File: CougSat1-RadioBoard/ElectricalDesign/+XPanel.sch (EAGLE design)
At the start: 51 parts, among them J1 ADCS Connector, J2 Low Gain +, J3 Low Gain -, J4 Low Gain Coax, J5 GPS Coax, J6 ADCS Connector, U2 MCP1501-18, U3 AD7291

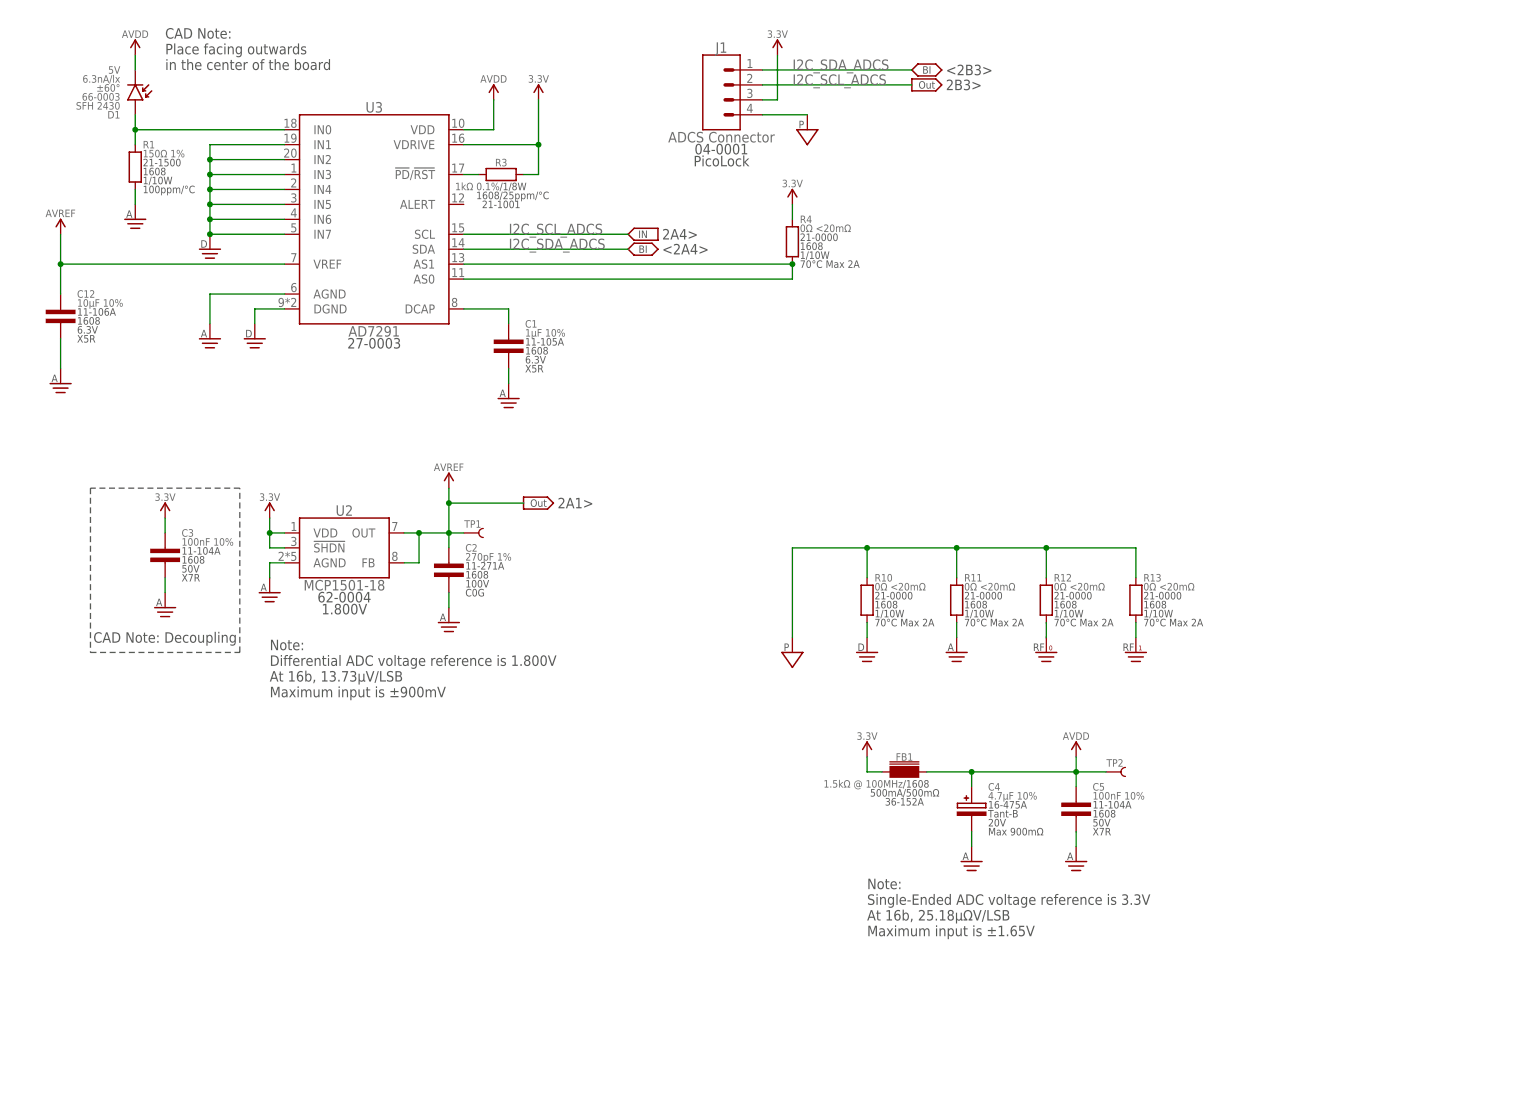
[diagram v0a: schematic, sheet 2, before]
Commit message: Added Thermistors
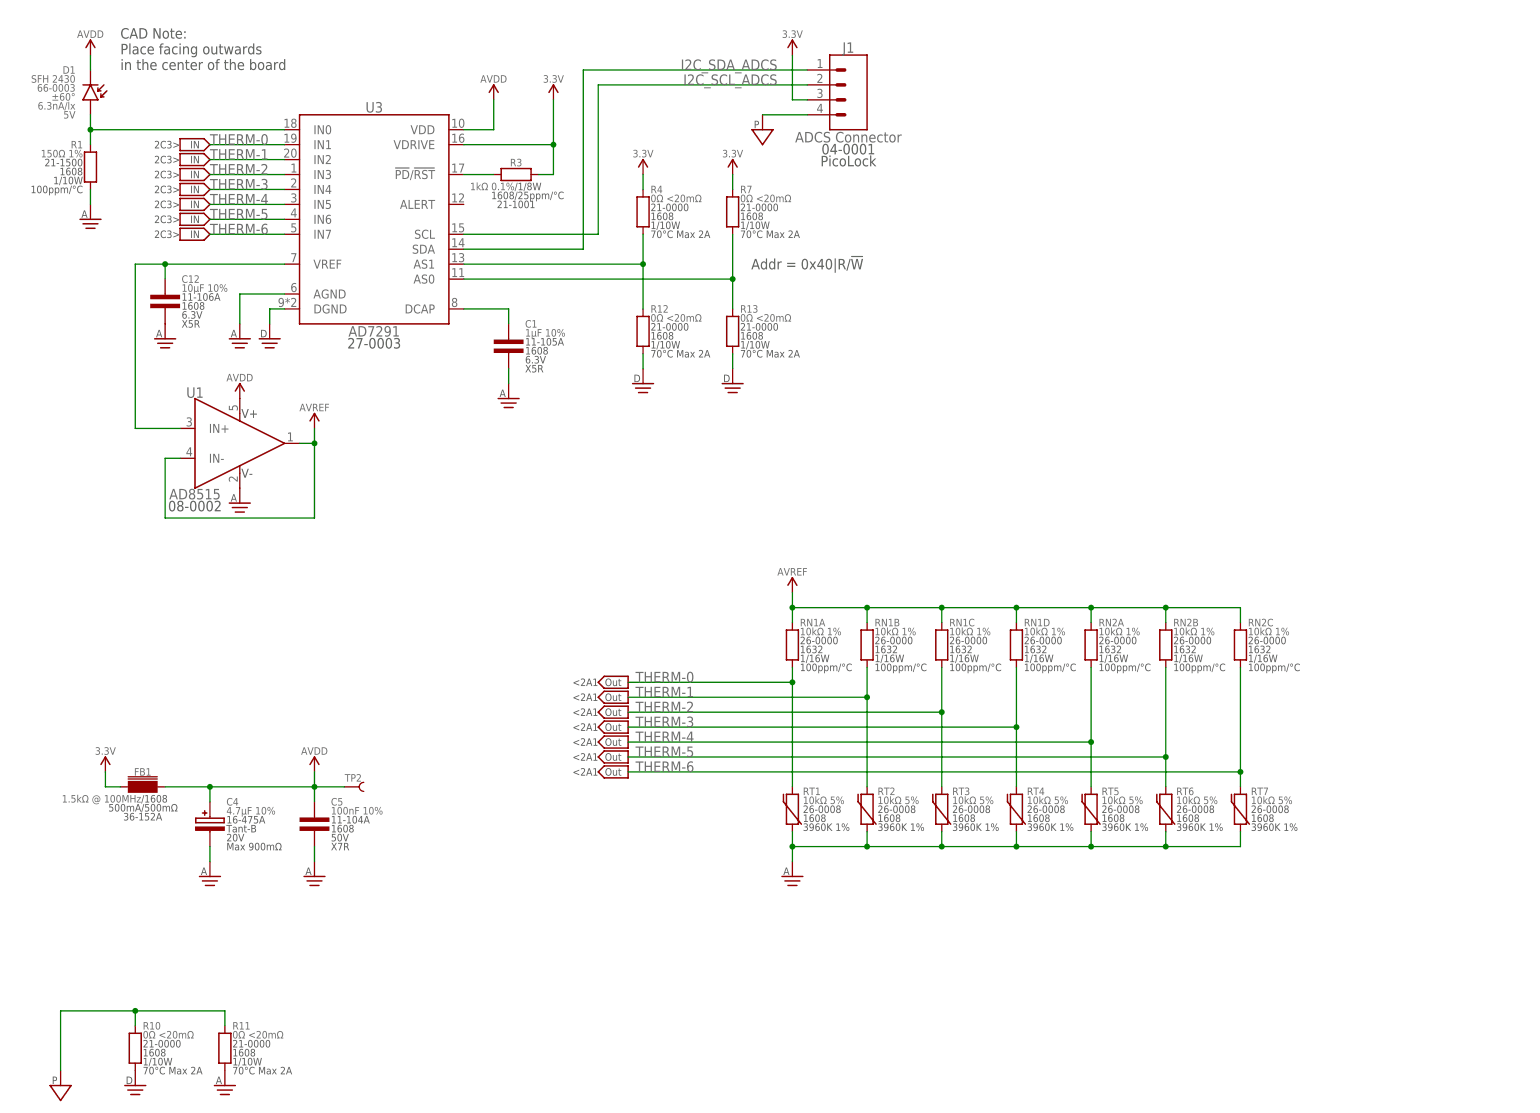
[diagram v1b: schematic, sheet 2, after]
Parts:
- removed C2: 270pF 1%, CougsInSpace-Capacitors:CAP-V-270PF-1608
- removed C3: 100nF 10%, CougsInSpace-Capacitors:CAP-V-100NF-1608
- removed TP1: TEST_POINT-THT-0.7, CougsInSpace-Connectors:TEST_POINT-THT-0.7
- removed U2: MCP1501-18, CougsInSpace-IC-Other:MCP1501-18E/RW
- added R7: 0Ω <20mΩ, CougsInSpace-Resistors:RES-V-0-1608
- added RN1, RN2: 10kΩ 1%, CougsInSpace-Resistors:RES-4-V-10K-1632
- added RT1, RT2, RT3, RT4, RT5, RT6, RT7: 10kΩ 5%, CougsInSpace-Resistors:THERMISTOR-V-10K-1608
- added U1: AD8515, CougsInSpace-IC-Amplifiers:OPAMP-1-AD8515
- J6: value ADCS Connector -> EPS Connector
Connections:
- removed net N$4: R4.1, U3.AS0, U3.AS1
- new net ADC_AS0: R13.2, R7.1, U3.AS0
- new net ADC_AS1: R12.2, R4.1, U3.AS1
- new net AVREF_UNBUF: C12.1, U1.IN+, U3.VREF
- new net THERM-0: RN1A.1, RT1.2, U3.IN1
- new net THERM-1: RN1B.1, RT2.2, U3.IN2
- new net THERM-2: RN1C.1, RT3.2, U3.IN3
- new net THERM-3: RN1D.1, RT4.2, U3.IN4
- new net THERM-4: RN2A.1, RT5.2, U3.IN5
- new net THERM-5: RN2B.1, RT6.2, U3.IN6
- new net THERM-6: RN2C.1, RT7.2, U3.IN7
- net 3.3V: now also R7.2; no longer C3.1, U2.!SHDN, U2.VDD
- net AGND: now also RT1.1, RT2.1, RT3.1, RT4.1, RT5.1, RT6.1, RT7.1, U1.V-; no longer C2.2, C3.2, U2.AGND
- net AVDD: now also U1.V+
- net AVREF: now also RN1A.2, RN1B.2, RN1C.2, RN1D.2, RN2A.2, RN2B.2, RN2C.2, U1.IN-, U1.OUT; no longer C12.1, C2.1, TP1.1, U2.FB, U2.OUT, U3.VREF
- net DGND: now also R12.1, R13.1; no longer U3.IN1, U3.IN2, U3.IN3, U3.IN4, U3.IN5, U3.IN6, U3.IN7
- net PGND: no longer R12.2, R13.2
- net RFGND-0: no longer R12.1
- net RFGND-1: no longer R13.1
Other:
- note added: "2C3>"
- note added: "<2A1"
- note added: "Addr = 0x40|R/!W"
- note added: "I²C"
- note added: "Note: The low gain antenna wraps around posts in these holes which shorts them together. When deployed, the deploy sense pin will be pulled high by the EPS"
- note added: "Page 1: Block Diagram Page 2: Photodiode & ADC Page 3: Antennae Page 4: Mechanical"
- note added: "Photodiode"
- note added: "Thermistors"
- note removed: "2A1>"
- note removed: "2A4>"
- note removed: "2B3>"
- note removed: "3A4>"
- note removed: "<2A4>"
- note removed: "<2B3>"
- note removed: "<3A5"
- note removed: "CAD Note: Decoupling"
- note removed: "Connector: To Avionics"
- note removed: "Note: Differential ADC voltage reference is 1.800V At 16b, 13.73µV/LSB Maximum input is ±900mV"
- note removed: "Note: Single-Ended ADC voltage reference is 3.3V At 16b, 25.18µΩV/LSB Maximum input is ±1.65V"
- note removed: "PC"
- note removed: "Page 1: Block Diagram Page 2: Photodiode Page 3: Antennae Page 4: Mechanical"
- note removed: "Photodiodes"
- moved on the sheet: AE1, C12, C4, C5, D1, FB1, H1, H2, H3, H4, J1, J2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

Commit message: Fixed formatting
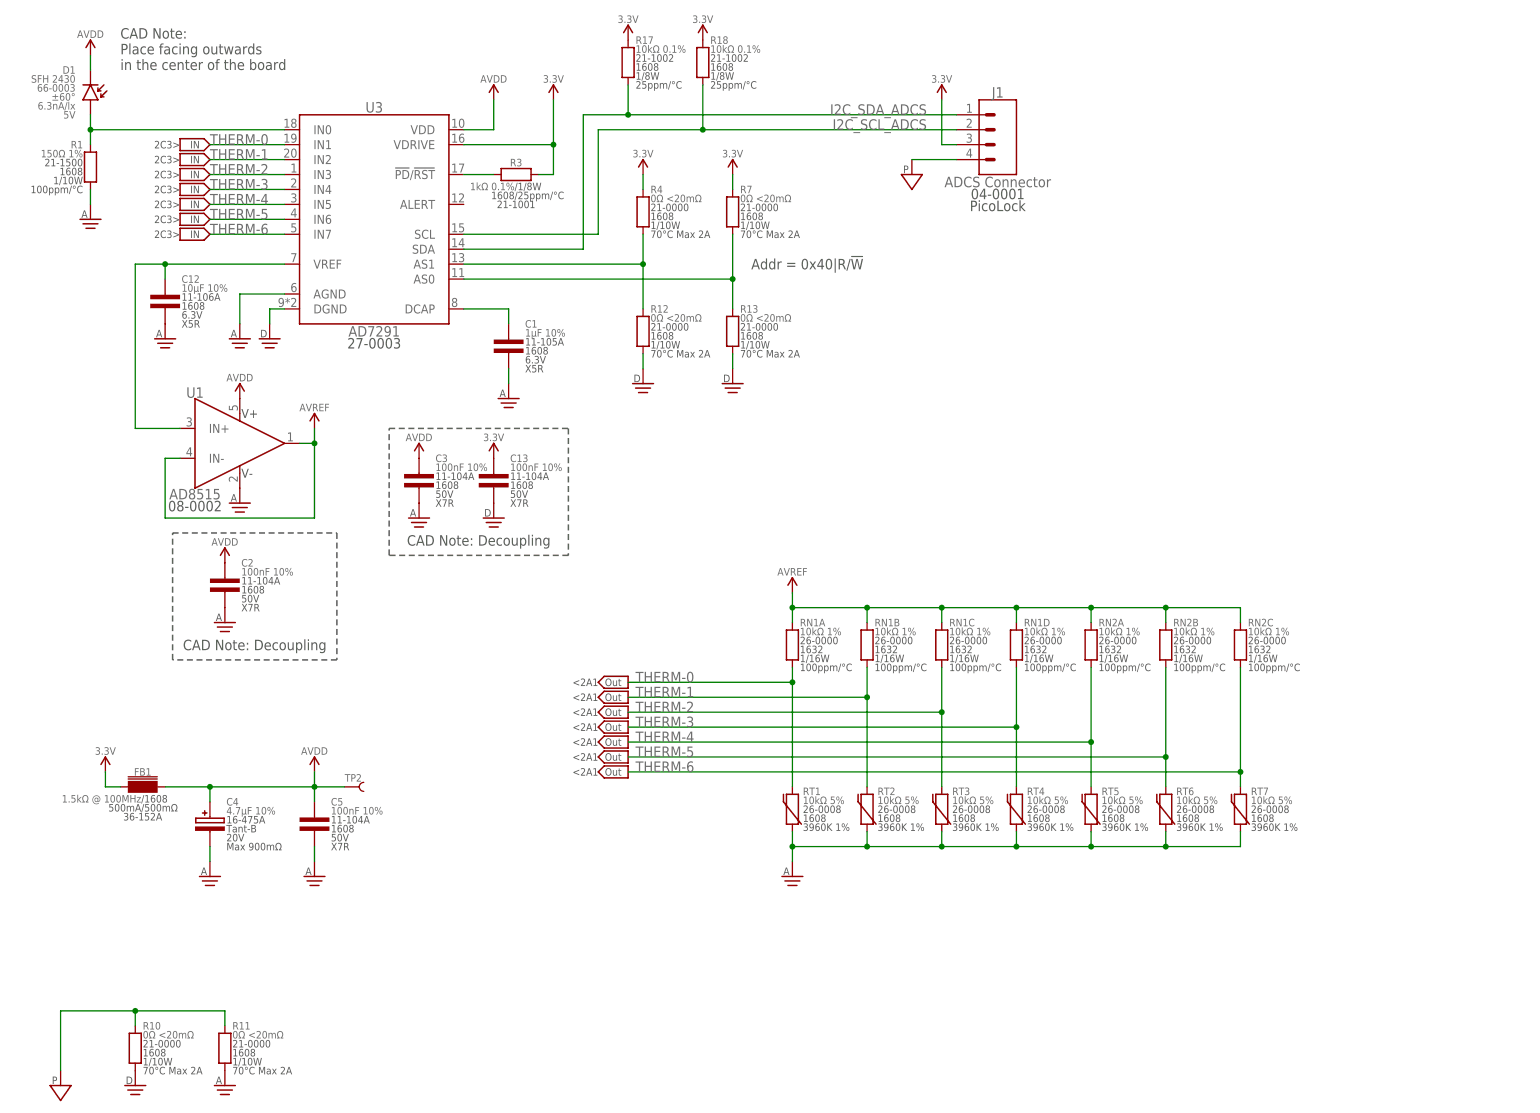
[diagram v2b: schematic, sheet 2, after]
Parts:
- added C13, C2, C3: 100nF 10%, CougsInSpace-Capacitors:CAP-V-100NF-1608
- added R17, R18: 10kΩ 0.1%, CougsInSpace-Resistors:RES-V-10K-1608
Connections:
- net 3.3V: now also C13.1, R17.2, R18.2
- net AGND: now also C2.2, C3.2
- net AVDD: now also C2.1, C3.1
- net DGND: now also C13.2
- net I2C_SCL_ADCS: now also R18.1
- net I2C_SDA_ADCS: now also R17.1
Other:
- note added: "CAD Note: Decoupling"
- moved on the sheet: J1

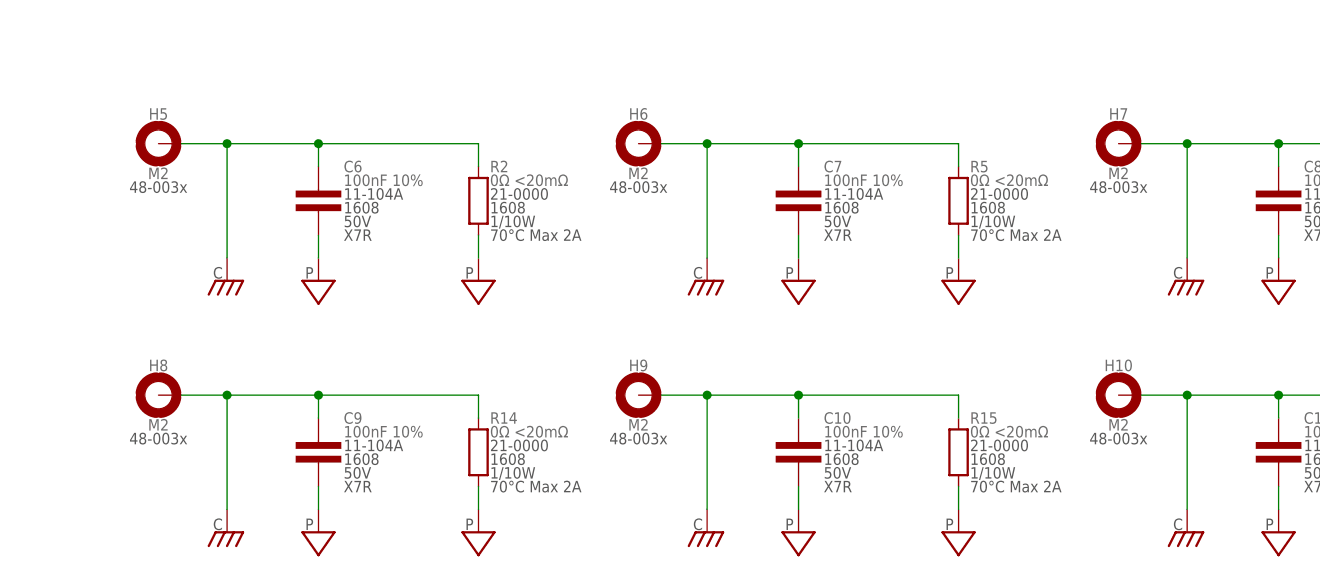
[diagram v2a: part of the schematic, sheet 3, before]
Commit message: Placed holes
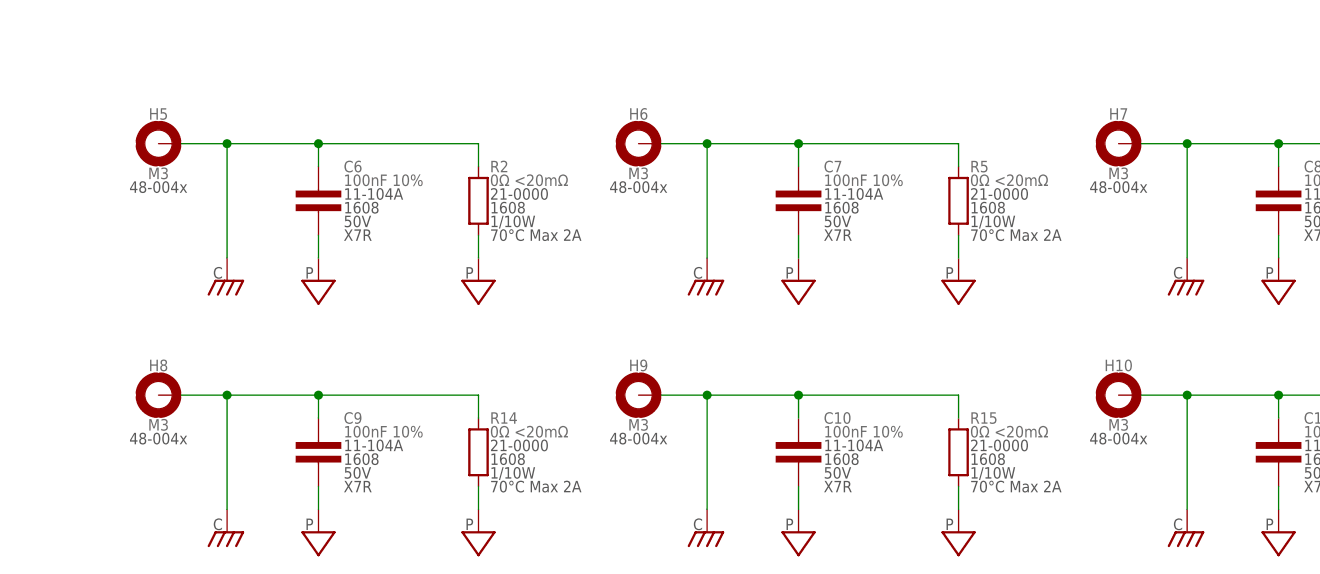
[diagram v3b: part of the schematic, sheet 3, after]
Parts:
- H10, H5, H6, H7, H8, H9: value M2 -> M3; device CougsInSpace-Hardware:MOUNTING_HOLE-2.2 -> CougsInSpace-Hardware:MOUNTING_HOLE-3.3
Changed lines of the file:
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@@
 </attributes>
 <variantdefs>
-<variantdef name="Main" current="yes"/>
+<variantdef name="Main"/>
 </variantdefs>
 <classes>
@@
 <part name="SUPPLY33" library="CougsInSpace-PowerSymbols" deviceset="AVDD" device=""/>
 <part name="TP2" library="CougsInSpace-Connectors" deviceset="TEST_POINT" device="-THT-0.7"/>
-<part name="H5" library="CougsInSpace-Hardware" deviceset="MOUNTING_HOLE" device="-2.2" value="M2"/>
+<part name="H5" library="CougsInSpace-Hardware" deviceset="MOUNTING_HOLE" device="-3.3" value="M3"/>
 <part name="C6" library="CougsInSpace-Capacitors" deviceset="CAP-V" device="-1608" technology="-100NF" value="100nF 10%"/>
 <part name="R2" library="CougsInSpace-Resistors" deviceset="RES-V" device="-1608" technology="-0" value="0Ω &lt;20mΩ"/>
@@
 <part name="SUPPLY35" library="CougsInSpace-PowerSymbols" deviceset="PGND" device=""/>
 <part name="SUPPLY36" library="CougsInSpace-PowerSymbols" deviceset="PGND" device=""/>
-<part name="H6" library="CougsInSpace-Hardware" deviceset="MOUNTING_HOLE" device="-2.2" value="M2"/>
+<part name="H6" library="CougsInSpace-Hardware" deviceset="MOUNTING_HOLE" device="-3.3" value="M3"/>
 <part name="C7" library="CougsInSpace-Capacitors" deviceset="CAP-V" device="-1608" technology="-100NF" value="100nF 10%"/>
 <part name="R5" library="CougsInSpace-Resistors" deviceset="RES-V" device="-1608" technology="-0" value="0Ω &lt;20mΩ"/>
@@
 <part name="SUPPLY38" library="CougsInSpace-PowerSymbols" deviceset="PGND" device=""/>
 <part name="SUPPLY39" library="CougsInSpace-PowerSymbols" deviceset="PGND" device=""/>
-<part name="H7" library="CougsInSpace-Hardware" deviceset="MOUNTING_HOLE" device="-2.2" value="M2"/>
+<part name="H7" library="CougsInSpace-Hardware" deviceset="MOUNTING_HOLE" device="-3.3" value="M3"/>
 <part name="C8" library="CougsInSpace-Capacitors" deviceset="CAP-V" device="-1608" technology="-100NF" value="100nF 10%"/>
 <part name="R6" library="CougsInSpace-Resistors" deviceset="RES-V" device="-1608" technology="-0" value="0Ω &lt;20mΩ"/>
@@
 <part name="SUPPLY41" library="CougsInSpace-PowerSymbols" deviceset="PGND" device=""/>
 <part name="SUPPLY42" library="CougsInSpace-PowerSymbols" deviceset="PGND" device=""/>
-<part name="H8" library="CougsInSpace-Hardware" deviceset="MOUNTING_HOLE" device="-2.2" value="M2"/>
+<part name="H8" library="CougsInSpace-Hardware" deviceset="MOUNTING_HOLE" device="-3.3" value="M3"/>
 <part name="C9" library="CougsInSpace-Capacitors" deviceset="CAP-V" device="-1608" technology="-100NF" value="100nF 10%"/>
 <part name="R14" library="CougsInSpace-Resistors" deviceset="RES-V" device="-1608" technology="-0" value="0Ω &lt;20mΩ"/>
@@
 <part name="SUPPLY44" library="CougsInSpace-PowerSymbols" deviceset="PGND" device=""/>
 <part name="SUPPLY45" library="CougsInSpace-PowerSymbols" deviceset="PGND" device=""/>
-<part name="H9" library="CougsInSpace-Hardware" deviceset="MOUNTING_HOLE" device="-2.2" value="M2"/>
+<part name="H9" library="CougsInSpace-Hardware" deviceset="MOUNTING_HOLE" device="-3.3" value="M3"/>
 <part name="C10" library="CougsInSpace-Capacitors" deviceset="CAP-V" device="-1608" technology="-100NF" value="100nF 10%"/>
 <part name="R15" library="CougsInSpace-Resistors" deviceset="RES-V" device="-1608" technology="-0" value="0Ω &lt;20mΩ"/>
@@
 <part name="SUPPLY47" library="CougsInSpace-PowerSymbols" deviceset="PGND" device=""/>
 <part name="SUPPLY48" library="CougsInSpace-PowerSymbols" deviceset="PGND" device=""/>
-<part name="H10" library="CougsInSpace-Hardware" deviceset="MOUNTING_HOLE" device="-2.2" value="M2"/>
+<part name="H10" library="CougsInSpace-Hardware" deviceset="MOUNTING_HOLE" device="-3.3" value="M3"/>
 <part name="C11" library="CougsInSpace-Capacitors" deviceset="CAP-V" device="-1608" technology="-100NF" value="100nF 10%"/>
 <part name="R16" library="CougsInSpace-Resistors" deviceset="RES-V" device="-1608" technology="-0" value="0Ω &lt;20mΩ"/>
